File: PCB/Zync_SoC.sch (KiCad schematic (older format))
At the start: 0 parts

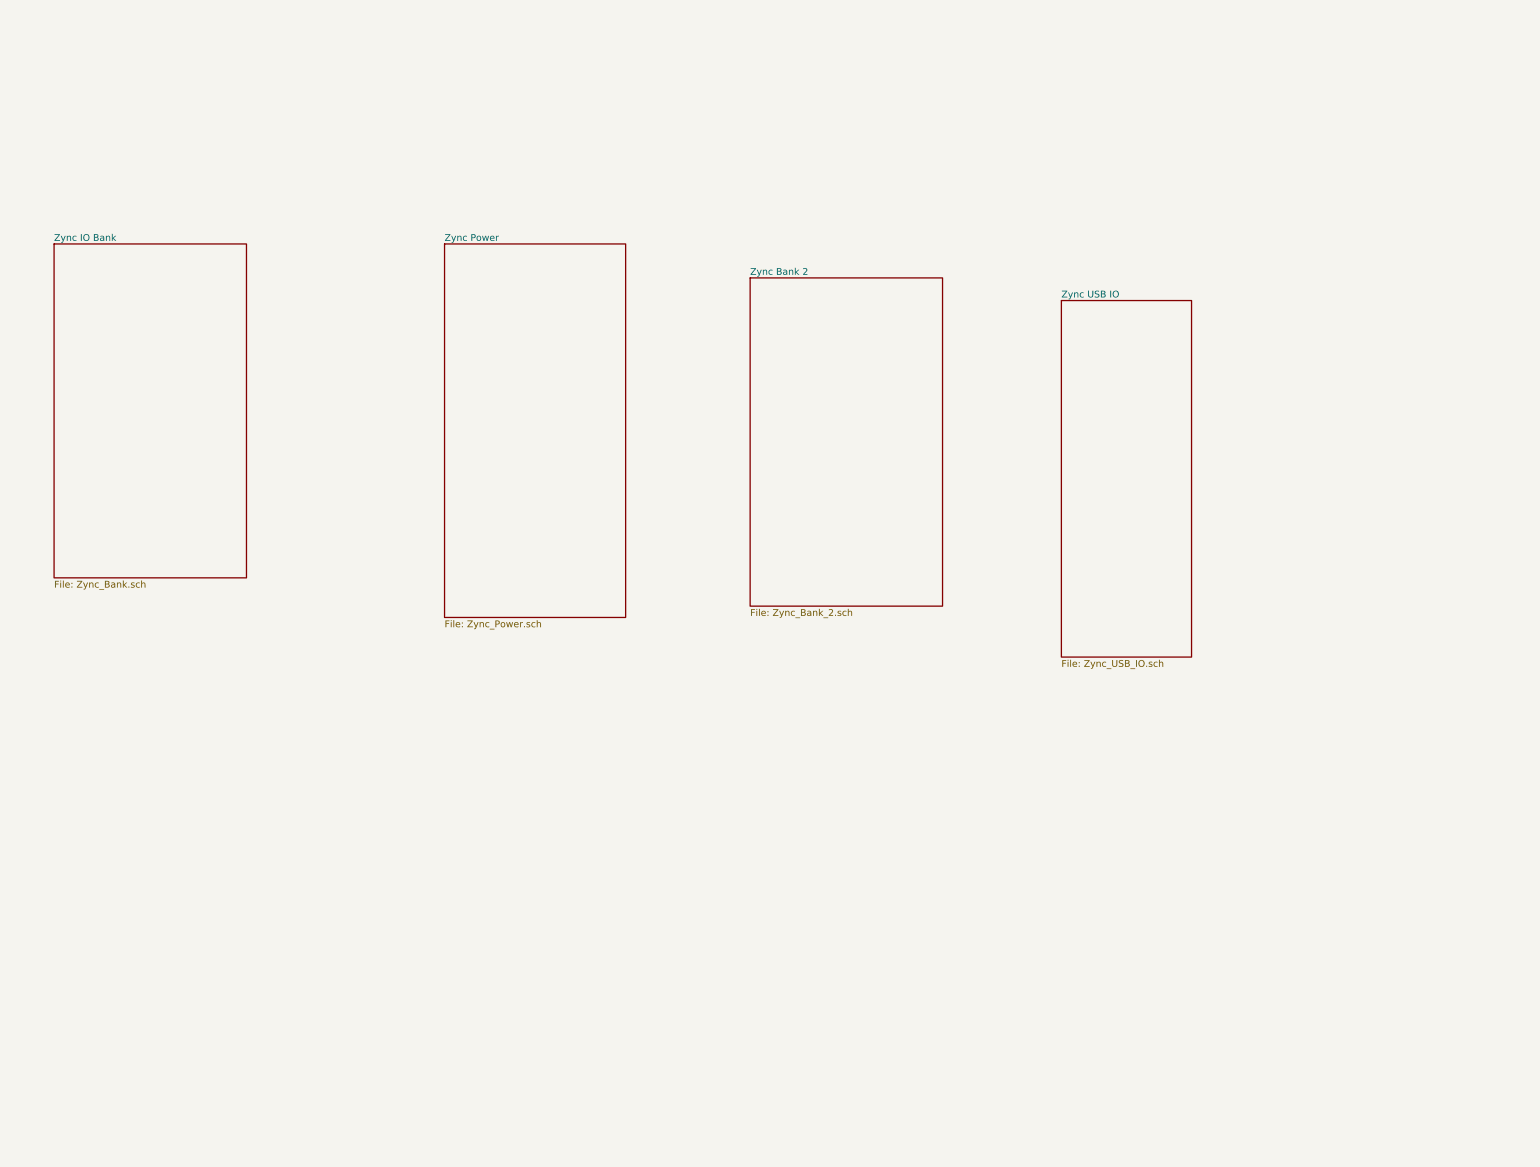
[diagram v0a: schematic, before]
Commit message: Progress
Datasheets added for regulators, regulators chosen, more datasheets
ralted to Zync 7000 added. Memory module chose footprint created and
datasheet added. Schematic work in progress. Project is slow going do to
th sheer amount of documenation to absorb on the Zync and makign high
pin count BGAs is tedious. More to follow soon.
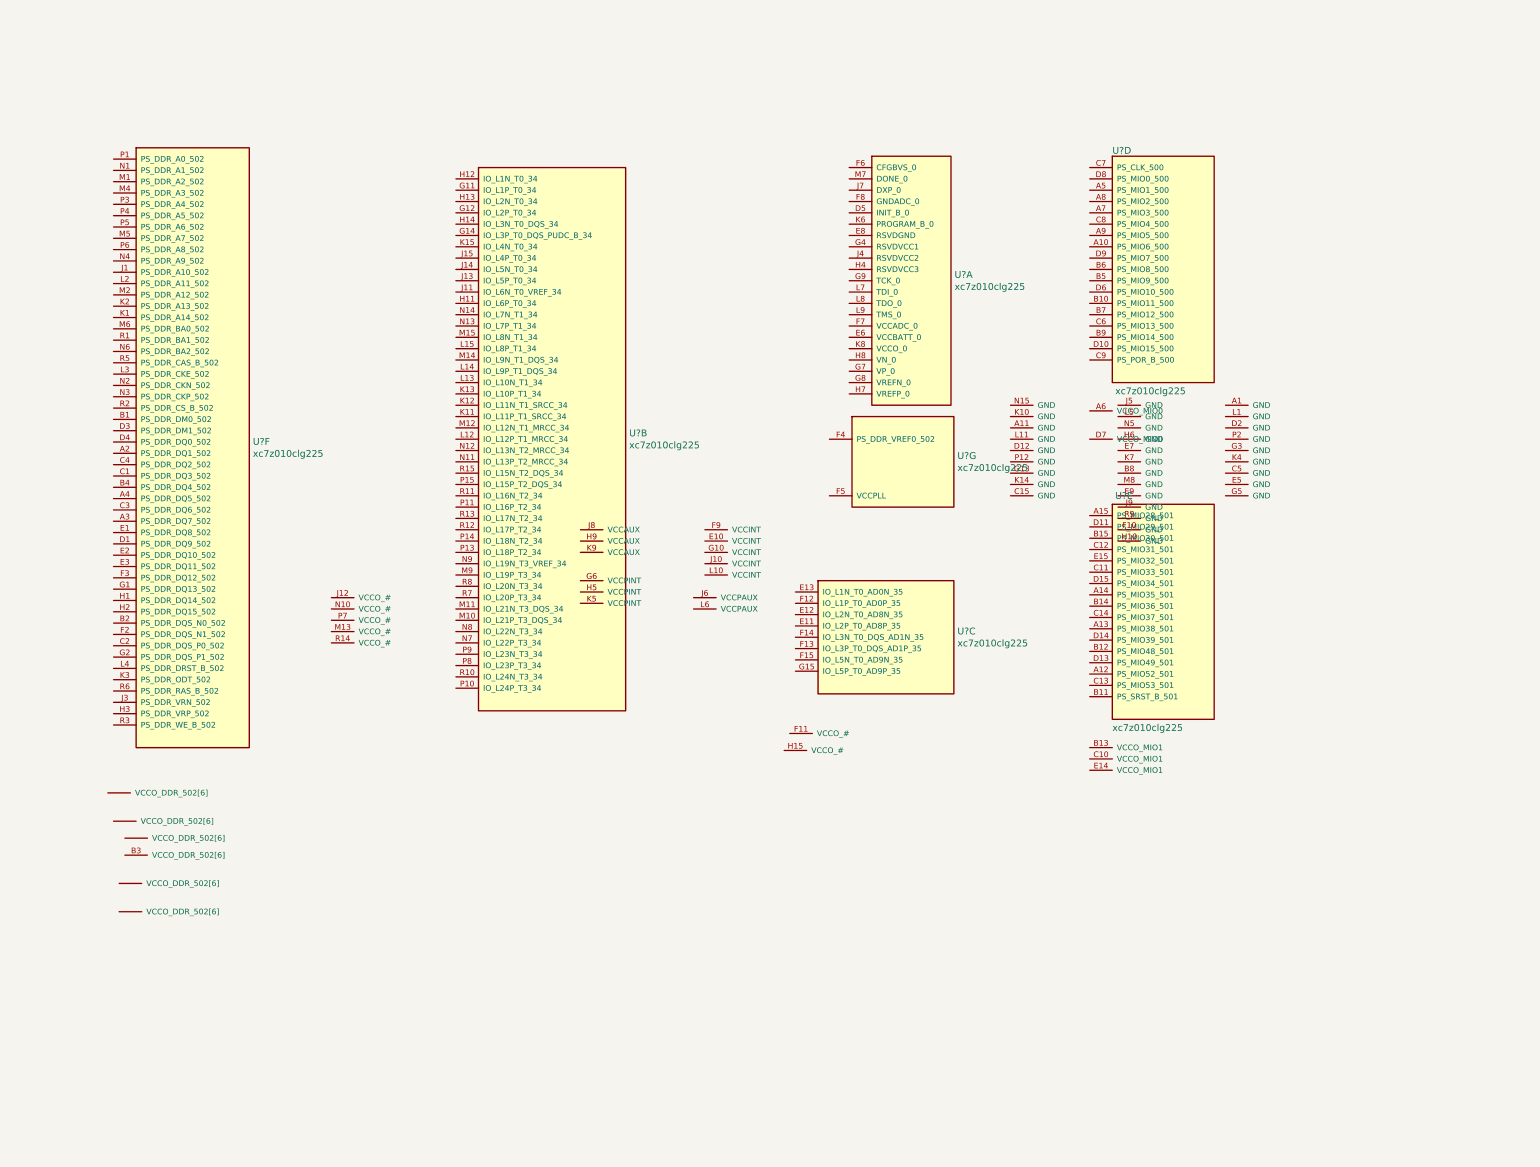
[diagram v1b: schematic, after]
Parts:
- added U? (x7): xc7z010clg225, symbol xc7z010clg225
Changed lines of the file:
@@
 LIBS:HydroPWNics_Lib
 LIBS:OnHand-Components-Sym
+LIBS:ZyncMV-cache
 EELAYER 25 0
 EELAYER END
 $Descr A4 11693 8268
 encoding utf-8
-Sheet 2 11
+Sheet 2 8
 Title ""
 Date ""
@@
 Comment4 ""
 $EndDescr
-$Sheet
-S 800  1450 1700 2950
-U 585AE648
-F0 "Zync IO Bank" 60
-F1 "Zync_Bank.sch" 60
-$EndSheet
-$Sheet
-S 4250 1450 1600 3300
-U 585AE67F
-F0 "Zync Power " 60
-F1 "Zync_Power.sch" 60
-$EndSheet
-$Sheet
-S 6950 1750 1700 2900
-U 585AE691
-F0 "Zync Bank 2" 60
-F1 "Zync_Bank_2.sch" 60
-$EndSheet
-$Sheet
-S 9700 1950 1150 3150
-U 585AE7ED
-F0 "Zync USB IO " 60
-F1 "Zync_USB_IO.sch" 60
-$EndSheet
+$Comp
+L xc7z010clg225 U?
+U 1 1 58868BF2
+P 7825 775
+F 0 "U?" H 8756 -172 60  0000 L CNN
+F 1 "xc7z010clg225" H 8756 -278 60  0000 L CNN
+F 2 "" H 7825 775 60  0001 C CNN
+F 3 "" H 7825 775 60  0001 C CNN
+	1    7825 775
+	1    0    0    -1
+$EndComp
+$Comp
+L xc7z010clg225 U?
+U 2 1 58868C64
+P 4350 875
+F 0 "U?" H 5881 -1372 60  0000 L CNN
+F 1 "xc7z010clg225" H 5881 -1478 60  0000 L CNN
+F 2 "" H 4350 875 60  0001 C CNN
+F 3 "" H 4350 875 60  0001 C CNN
+	2    4350 875
+	1    0    0    -1
+$EndComp
+$Comp
+L xc7z010clg225 U?
+U 3 1 58868CE8
+P 7350 4525
+F 0 "U?" H 8781 4178 60  0000 L CNN
+F 1 "xc7z010clg225" H 8781 4072 60  0000 L CNN
+F 2 "" H 7350 4525 60  0001 C CNN
+F 3 "" H 7350 4525 60  0001 C CNN
+	3    7350 4525
+	1    0    0    -1
+$EndComp
+$Comp
+L xc7z010clg225 U?
+U 4 1 58868D6E
+P 9950 775
+F 0 "U?" H 10150 925 60  0000 L CNN
+F 1 "xc7z010clg225" H 10175 -1200 60  0000 L CNN
+F 2 "" H 9950 775 60  0001 C CNN
+F 3 "" H 9950 775 60  0001 C CNN
+	4    9950 775
+	1    0    0    -1
+$EndComp
+$Comp
+L xc7z010clg225 U?
+U 5 1 58868DD8
+P 9950 3850
+F 0 "U?" H 10175 4025 60  0000 L CNN
+F 1 "xc7z010clg225" H 10150 1975 60  0000 L CNN
+F 2 "" H 9950 3850 60  0001 C CNN
+F 3 "" H 9950 3850 60  0001 C CNN
+	5    9950 3850
+	1    0    0    -1
+$EndComp
+$Comp
+L xc7z010clg225 U?
+U 6 1 58868E6E
+P 1325 700
+F 0 "U?" H 2556 -1797 60  0000 L CNN
+F 1 "xc7z010clg225" H 2556 -1903 60  0000 L CNN
+F 2 "" H 1325 700 60  0001 C CNN
+F 3 "" H 1325 700 60  0001 C CNN
+	6    1325 700
+	1    0    0    -1
+$EndComp
+$Comp
+L xc7z010clg225 U?
+U 7 1 58868F62
+P 7650 3075
+F 0 "U?" H 8781 2828 60  0000 L CNN
+F 1 "xc7z010clg225" H 8781 2722 60  0000 L CNN
+F 2 "" H 7650 3075 60  0001 C CNN
+F 3 "" H 7650 3075 60  0001 C CNN
+	7    7650 3075
+	1    0    0    -1
+$EndComp
 $EndSCHEMATC

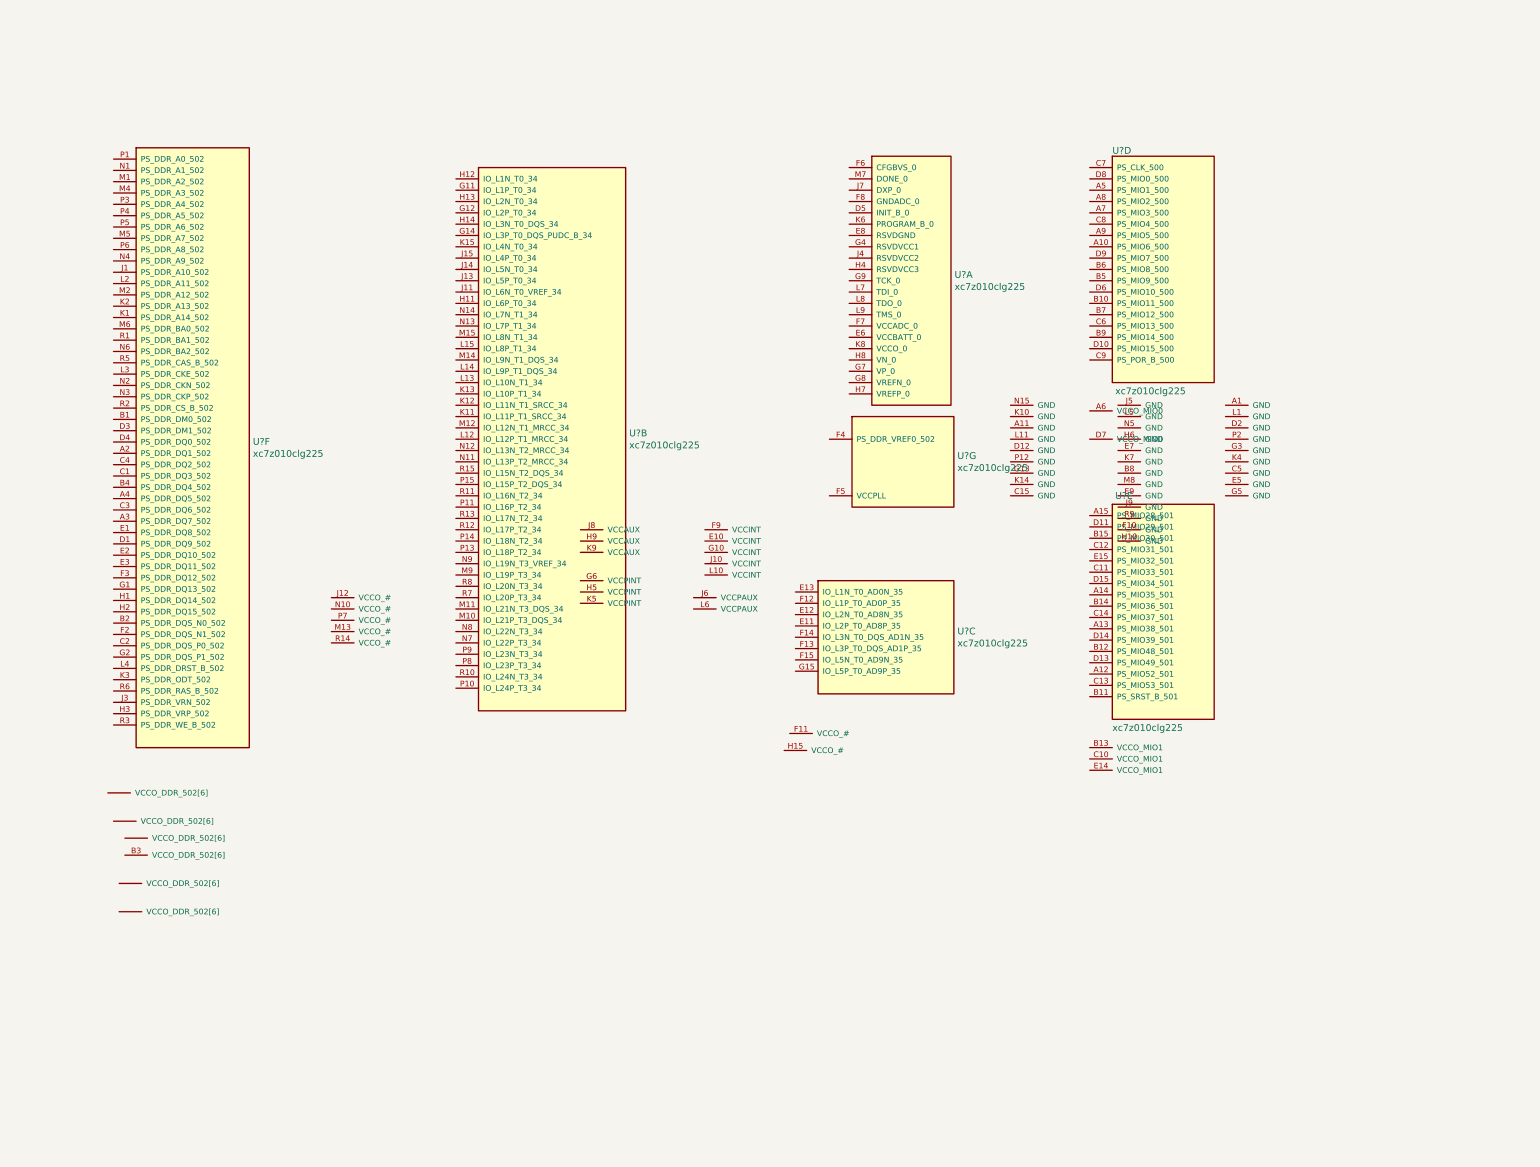
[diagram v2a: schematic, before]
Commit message: Power
Power topology change. Power system schematic spans 3 pages. two for the
PMIC that supplies the SoC and the DDR3L and an addional page covering
input stage and DCDC regulators for other voltages, particularly for the
off board lighting module.
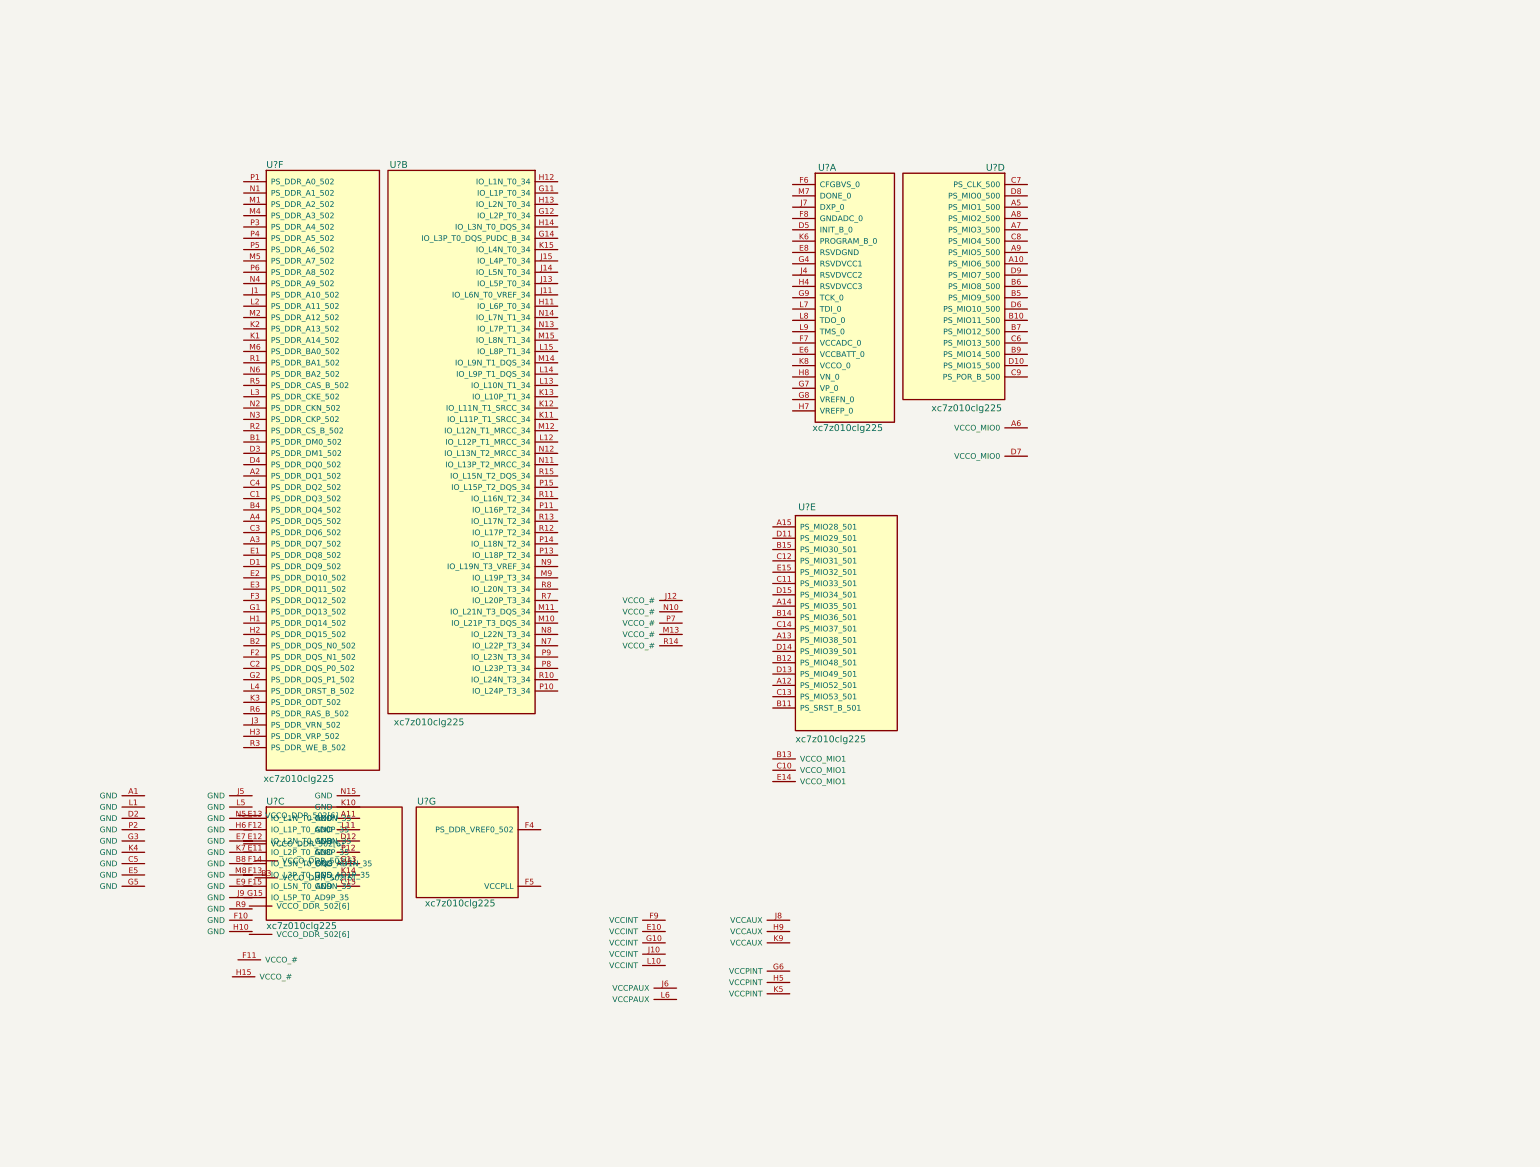
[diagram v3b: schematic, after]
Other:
- moved on the sheet: U?A, U?B, U?C, U?D, U?E, U?F, U?G
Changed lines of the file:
@@
 $Descr A4 11693 8268
 encoding utf-8
-Sheet 2 8
+Sheet 2 9
 Title ""
 Date "2016-12-23"
@@
 L xc7z010clg225 U?
 U 1 1 58868BF2
-P 7825 775
-F 0 "U?" H 8756 -172 60  0000 L CNN
-F 1 "xc7z010clg225" H 8756 -278 60  0000 L CNN
-F 2 "" H 7825 775 60  0001 C CNN
-F 3 "" H 7825 775 60  0001 C CNN
-	1    7825 775
+P 7325 925
+F 0 "U?" H 7550 1075 60  0000 L CNN
+F 1 "xc7z010clg225" H 7500 -1225 60  0000 L CNN
+F 2 "" H 7325 925 60  0001 C CNN
+F 3 "" H 7325 925 60  0001 C CNN
+	1    7325 925
 	1    0    0    -1
 $EndComp
@@
 L xc7z010clg225 U?
 U 2 1 58868C64
-P 4350 875
-F 0 "U?" H 5881 -1372 60  0000 L CNN
-F 1 "xc7z010clg225" H 5881 -1478 60  0000 L CNN
-F 2 "" H 4350 875 60  0001 C CNN
-F 3 "" H 4350 875 60  0001 C CNN
-	2    4350 875
-	1    0    0    -1
+P 5250 900
+F 0 "U?" H 6575 1050 60  0000 L CNN
+F 1 "xc7z010clg225" H 6075 -3875 60  0000 L CNN
+F 2 "" H 5250 900 60  0001 C CNN
+F 3 "" H 5250 900 60  0001 C CNN
+	2    5250 900
+	-1   0    0    -1
 $EndComp
 $Comp
 L xc7z010clg225 U?
 U 3 1 58868CE8
-P 7350 4525
-F 0 "U?" H 8781 4178 60  0000 L CNN
-F 1 "xc7z010clg225" H 8781 4072 60  0000 L CNN
-F 2 "" H 7350 4525 60  0001 C CNN
-F 3 "" H 7350 4525 60  0001 C CNN
-	3    7350 4525
+P 2475 6525
+F 0 "U?" H 2675 6675 60  0000 L CNN
+F 1 "xc7z010clg225" H 2675 5575 60  0000 L CNN
+F 2 "" H 2475 6525 60  0001 C CNN
+F 3 "" H 2475 6525 60  0001 C CNN
+	3    2475 6525
 	1    0    0    -1
 $EndComp
@@
 L xc7z010clg225 U?
 U 4 1 58868D6E
-P 9950 775
-F 0 "U?" H 10150 925 60  0000 L CNN
-F 1 "xc7z010clg225" H 10175 -1200 60  0000 L CNN
-F 2 "" H 9950 775 60  0001 C CNN
-F 3 "" H 9950 775 60  0001 C CNN
-	4    9950 775
-	1    0    0    -1
+P 9400 925
+F 0 "U?" H 9600 1075 60  0000 L CNN
+F 1 "xc7z010clg225" H 9625 -1050 60  0000 L CNN
+F 2 "" H 9400 925 60  0001 C CNN
+F 3 "" H 9400 925 60  0001 C CNN
+	4    9400 925
+	-1   0    0    -1
 $EndComp
 $Comp
 L xc7z010clg225 U?
 U 5 1 58868DD8
-P 9950 3850
-F 0 "U?" H 10175 4025 60  0000 L CNN
-F 1 "xc7z010clg225" H 10150 1975 60  0000 L CNN
-F 2 "" H 9950 3850 60  0001 C CNN
-F 3 "" H 9950 3850 60  0001 C CNN
-	5    9950 3850
+P 7150 3950
+F 0 "U?" H 7375 4125 60  0000 L CNN
+F 1 "xc7z010clg225" H 7350 2075 60  0000 L CNN
+F 2 "" H 7150 3950 60  0001 C CNN
+F 3 "" H 7150 3950 60  0001 C CNN
+	5    7150 3950
 	1    0    0    -1
 $EndComp
@@
 L xc7z010clg225 U?
 U 6 1 58868E6E
-P 1325 700
-F 0 "U?" H 2556 -1797 60  0000 L CNN
-F 1 "xc7z010clg225" H 2556 -1903 60  0000 L CNN
-F 2 "" H 1325 700 60  0001 C CNN
-F 3 "" H 1325 700 60  0001 C CNN
-	6    1325 700
+P 2475 900
+F 0 "U?" H 2675 1050 60  0000 L CNN
+F 1 "xc7z010clg225" H 2650 -4375 60  0000 L CNN
+F 2 "" H 2475 900 60  0001 C CNN
+F 3 "" H 2475 900 60  0001 C CNN
+	6    2475 900
 	1    0    0    -1
 $EndComp
@@
 L xc7z010clg225 U?
 U 7 1 58868F62
-P 7650 3075
-F 0 "U?" H 8781 2828 60  0000 L CNN
-F 1 "xc7z010clg225" H 8781 2722 60  0000 L CNN
-F 2 "" H 7650 3075 60  0001 C CNN
-F 3 "" H 7650 3075 60  0001 C CNN
-	7    7650 3075
-	1    0    0    -1
+P 5100 6525
+F 0 "U?" H 6025 6675 60  0000 L CNN
+F 1 "xc7z010clg225" H 5500 5775 60  0000 L CNN
+F 2 "" H 5100 6525 60  0001 C CNN
+F 3 "" H 5100 6525 60  0001 C CNN
+	7    5100 6525
+	-1   0    0    -1
 $EndComp
 $EndSCHEMATC
